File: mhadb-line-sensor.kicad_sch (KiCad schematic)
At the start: 93 parts, among them J1 Conn_01x04, J2 TC2030, J3 Conn_01x04_Pin, J4 Conn_01x04_Pin, SW1 SW_Push, SW2 SW_Push, SW3 SW_Push, SW4 SW_Push, U1 STM32F103C8Tx, U10 QRE1113GR, U11 QRE1113GR, U12 QRE1113GR, U2 QRE1113GR, U3 SN65HVD230, U4 QRE1113GR, U5 QRE1113GR, U6 QRE1113GR, U7 QRE1113GR, U8 QRE1113GR, U9 QRE1113GR, Y1 8M

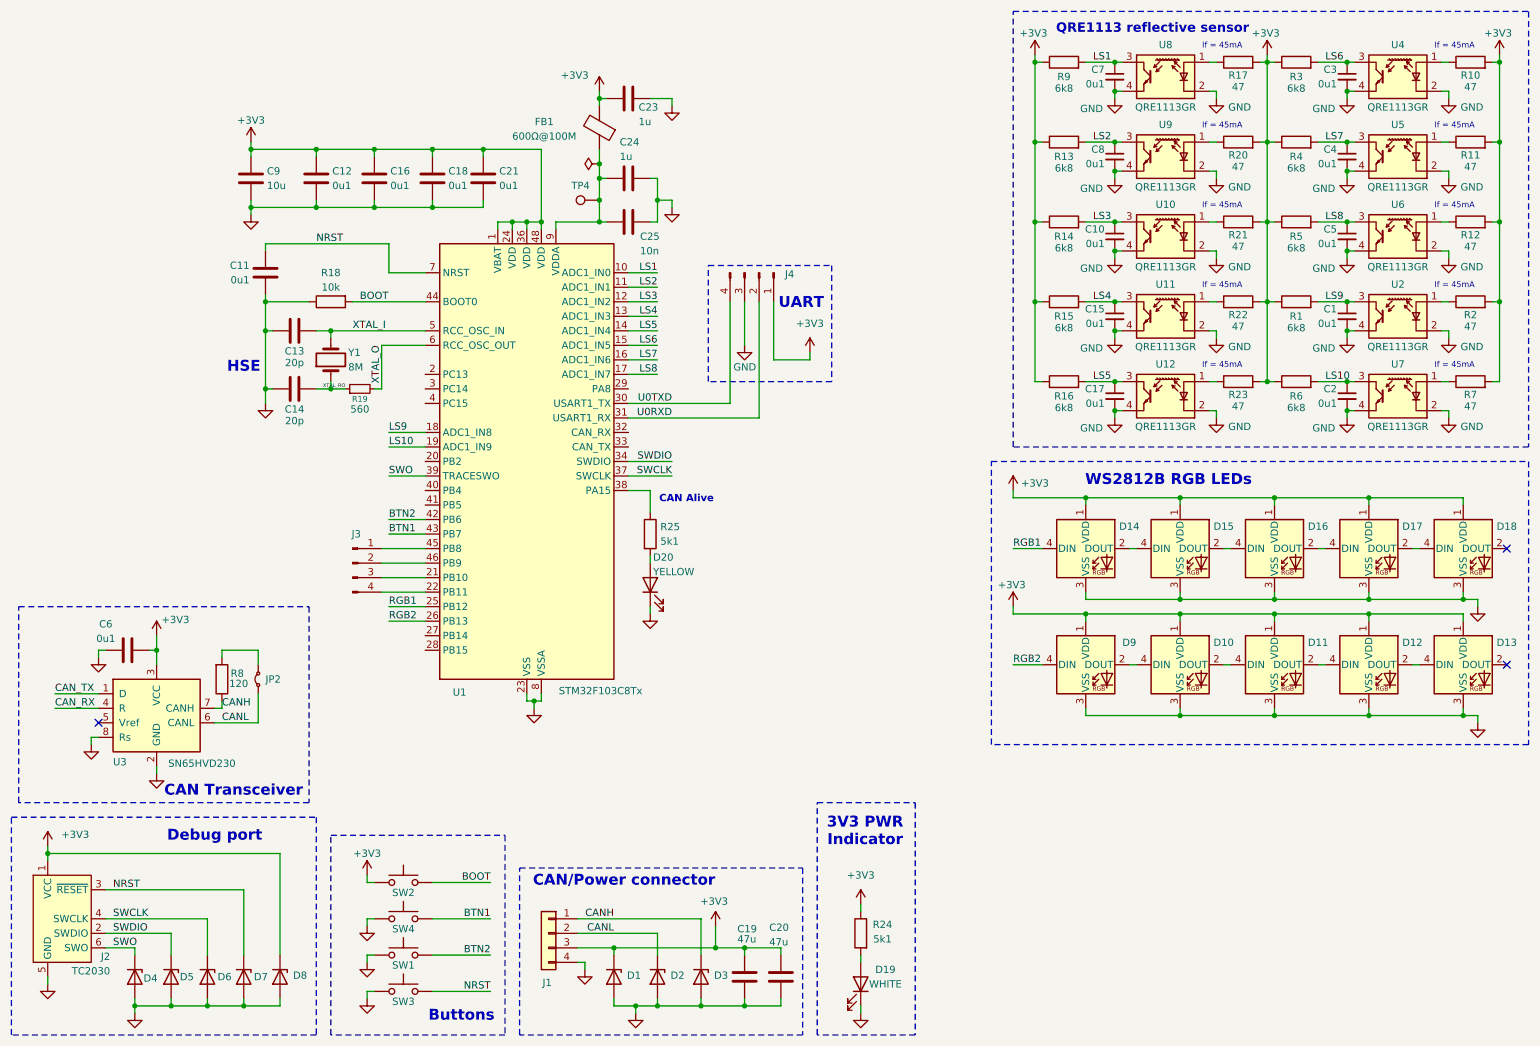
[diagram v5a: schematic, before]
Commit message: schem: switch to 5v architecture and add 3v3 LDO
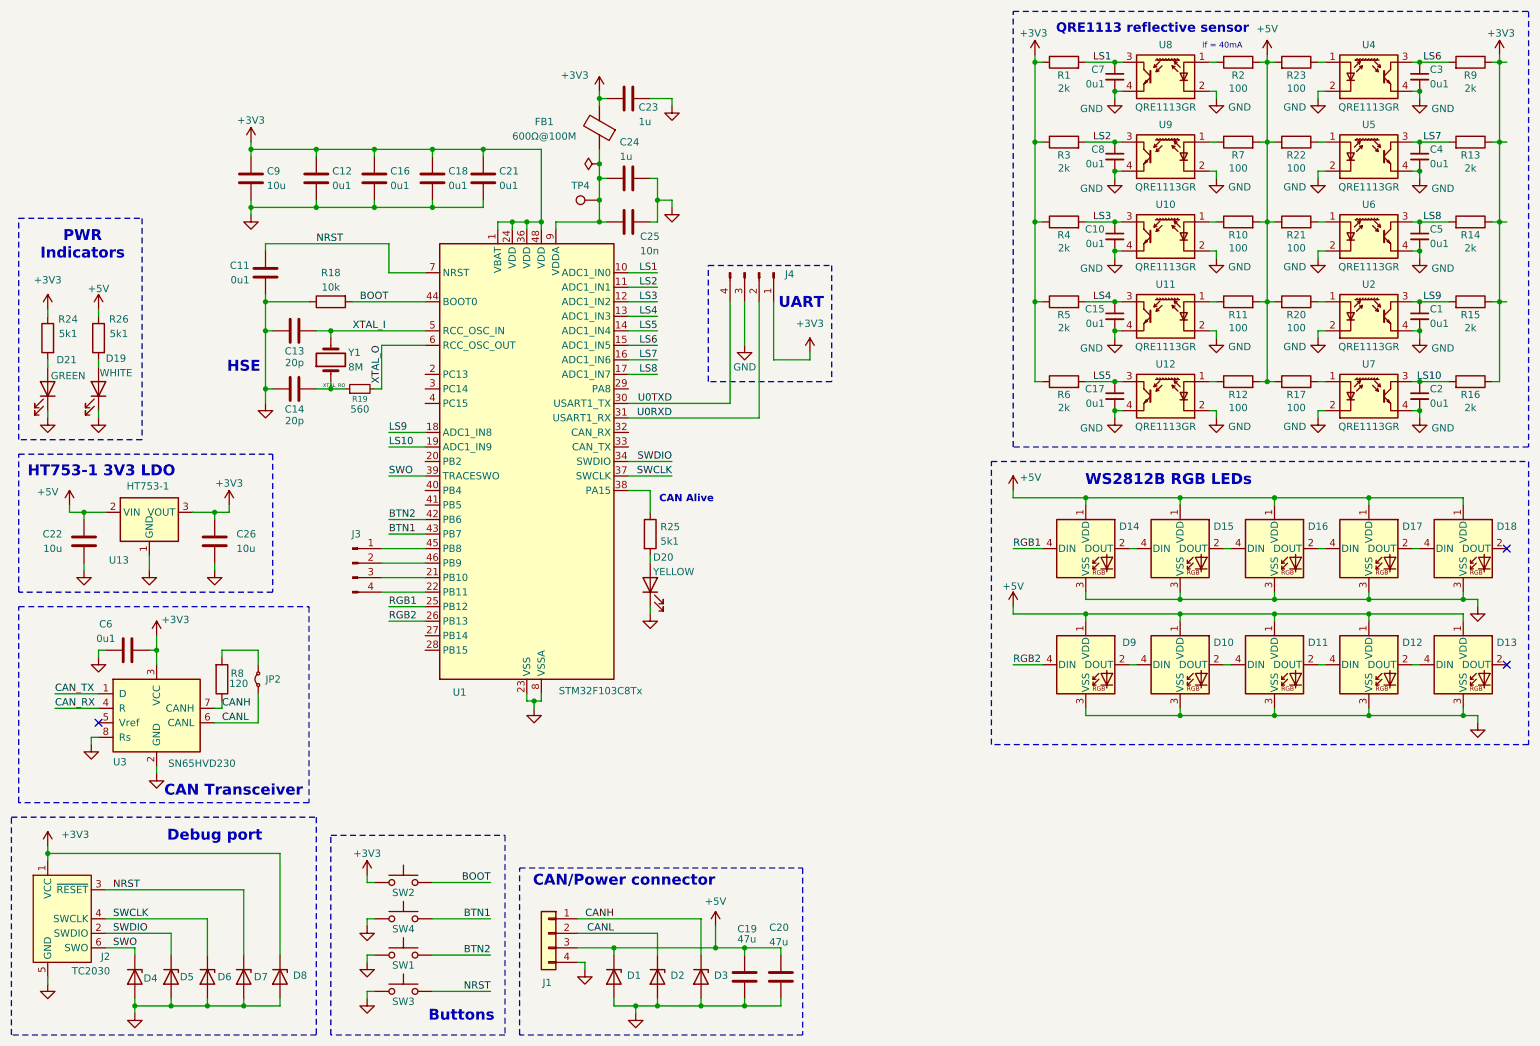
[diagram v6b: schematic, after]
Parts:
- added C22, C26: 10u, Capacitor_SMD:C_0805_2012Metric, symbol Device:C
- added D21: GREEN, LED_SMD:LED_0805_2012Metric, symbol Device:LED
- added R26: 5k1, Resistor_SMD:R_0402_1005Metric, symbol Device:R
- added U13: HT753-1, Package_TO_SOT_SMD:SOT-89-3, symbol Regulator_Linear:HT75xx-1-SOT89
- R1, R13, R14, R15, R16, R3, R4, R5, R6, R9: value 6k8 -> 2k; JLCPCB Part # C23212 -> C4190; Manufacturer Part Number 0603WAF6801T5E -> 0603WAF2201T5E
- R10, R11, R12, R17, R2, R20, R21, R22, R23, R7: value 47 -> 100; footprint Resistor_SMD:R_0603_1608Metric -> Capacitor_SMD:C_1206_3216Metric; JLCPCB Part # C23182 -> C17901; Manufacturer Part Number 0603WAF470JT5E -> 1206W4F1000T5E
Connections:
- net +3V3: now also C26.1, U13.3 (VOUT); no longer C19.1, C20.1, D1.1 (K), D10.1 (VDD), D11.1 (VDD), D12.1 (VDD), D13.1 (VDD), D14.1 (VDD), D15.1 (VDD), D16.1 (VDD), D17.1 (VDD), D18.1 (VDD), D9.1 (VDD), J1.3 (Pin_3), R10.2, R11.2, R12.2, R17.2, R2.2, R20.2, R21.2, R22.2, R23.2, R7.2
- net GND: now also C22.2, C26.2, D21.1 (K), U13.1 (GND)
- net LS1: now also R1.2; no longer R9.2
- net LS10: now also R16.2; no longer R6.2
- net LS2: now also R3.2; no longer R13.2
- net LS3: now also R4.2; no longer R14.2
- net LS4: now also R5.2; no longer R15.2
- net LS5: now also R6.2; no longer R16.2
- net LS6: now also R9.2; no longer R3.2
- net LS7: now also R13.2; no longer R4.2
- net LS8: now also R14.2; no longer R5.2
- net LS9: now also R15.2; no longer R1.2
- net at R23.1: now also U4.1 (A); no longer U12.1 (A)
- net at R10.1: now also U10.1 (A); no longer U4.1 (A)
- net at D19.2 (A): now also R26.2; no longer R24.2
- net at U2.1 (A): now also R20.1; no longer R2.1
- net at R22.1: now also U5.1 (A); no longer U11.1 (A)
- net at R11.1: now also U11.1 (A); no longer U5.1 (A)
- net at R12.1: now also U12.1 (A); no longer U6.1 (A)
- net at R21.1: now also U6.1 (A); no longer U10.1 (A)
- net at U8.1 (A): now also R2.1; no longer R17.1
- net at U9.1 (A): now also R7.1; no longer R20.1
- net at U7.1 (A): now also R17.1; no longer R7.1
- new net: D21.2 (A), R24.2
- new net +5V: C19.1, C20.1, C22.1, D1.1 (K), D10.1 (VDD), D11.1 (VDD), D12.1 (VDD), D13.1 (VDD), D14.1 (VDD), D15.1 (VDD), D16.1 (VDD), D17.1 (VDD), D18.1 (VDD), D9.1 (VDD), J1.3 (Pin_3), R10.2, R11.2, R12.2, R17.2, R2.2, R20.2, R21.2, R22.2, R23.2, R26.1, R7.2, U13.2 (VIN)
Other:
- note added: "HT753-1 3V3 LDO"
- note added: "If = 40mA"
- note added: "PWR Indicators"
- note removed: "3V3 PWR Indicator"
- note removed: "If = 45mA"
- moved on the sheet: C1, C2, C3, C4, C5, D19, R24, U2, U4, U5, U6, U7

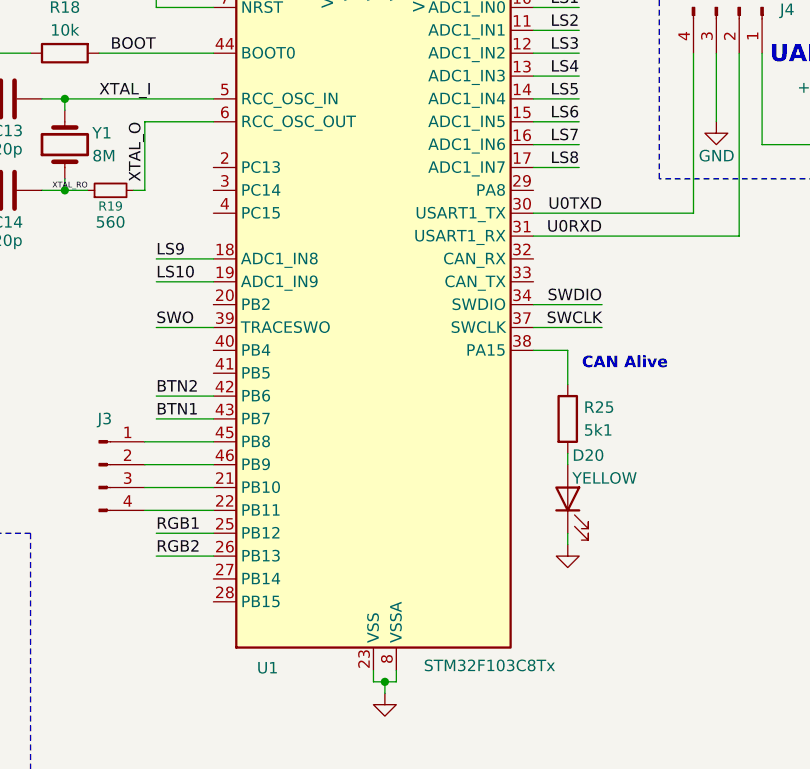
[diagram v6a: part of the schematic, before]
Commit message: schem: add no connects
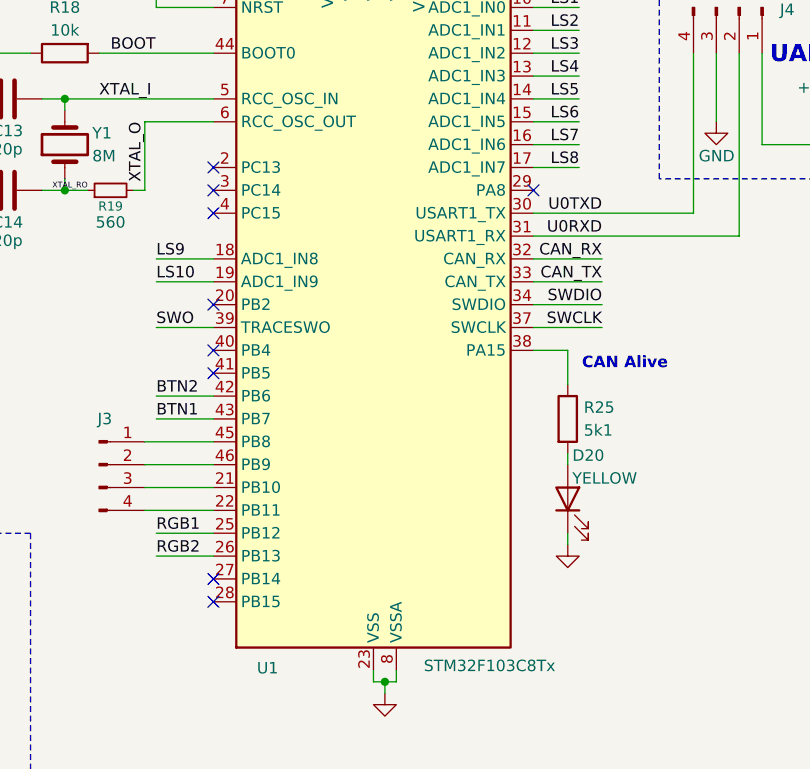
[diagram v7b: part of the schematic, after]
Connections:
- net CAN_RX: now also U1.32 (PA11)
- net CAN_TX: now also U1.33 (PA12)
- no-connect marks 3 -> 12
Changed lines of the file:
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@@
 	)
 	(no_connect
+		(at 87.63 82.55)
+	)
+	(no_connect
+		(at 87.63 85.09)
+	)
+	(no_connect
+		(at 87.63 102.87)
+	)
+	(no_connect
+		(at 123.19 82.55)
+	)
+	(no_connect
 		(at 276.86 130.81)
 	)
 	(no_connect
+		(at 87.63 100.33)
+	)
+	(no_connect
 		(at 30.48 140.97)
 	)
 	(no_connect
+		(at 87.63 80.01)
+	)
+	(no_connect
 		(at 276.86 110.49)
 	)
+	(no_connect
+		(at 87.63 128.27)
+	)
+	(no_connect
+		(at 87.63 125.73)
+	)
+	(no_connect
+		(at 87.63 95.25)
+	)
 	(wire
 		(pts
@@
 	(wire
 		(pts
+			(xy 130.81 92.71) (xy 123.19 92.71)
+		)
+		(stroke
+			(width 0)
+			(type default)
+		)
+	)
+	(wire
+		(pts
 			(xy 194.31 67.31) (xy 195.58 67.31)
 		)
@@
 	(wire
 		(pts
+			(xy 130.81 90.17) (xy 123.19 90.17)
+		)
+		(stroke
+			(width 0)
+			(type default)
+		)
+	)
+	(wire
+		(pts
 			(xy 81.28 92.71) (xy 87.63 92.71)
 		)
@@
 	)
 	(label "CAN_RX"
+		(at 130.81 90.17 180)
+		(effects
+			(font
+				(size 1.27 1.27)
+			)
+			(justify right bottom)
+		)
+	)
+	(label "CAN_RX"
 		(at 22.86 138.43 0)
 		(effects
@@
 		(effects
 			(font
+				(size 1.27 1.27)
+			)
+			(justify right bottom)
+		)
+	)
+	(label "CAN_TX"
+		(at 130.81 92.71 180)
+		(effects
+			(font

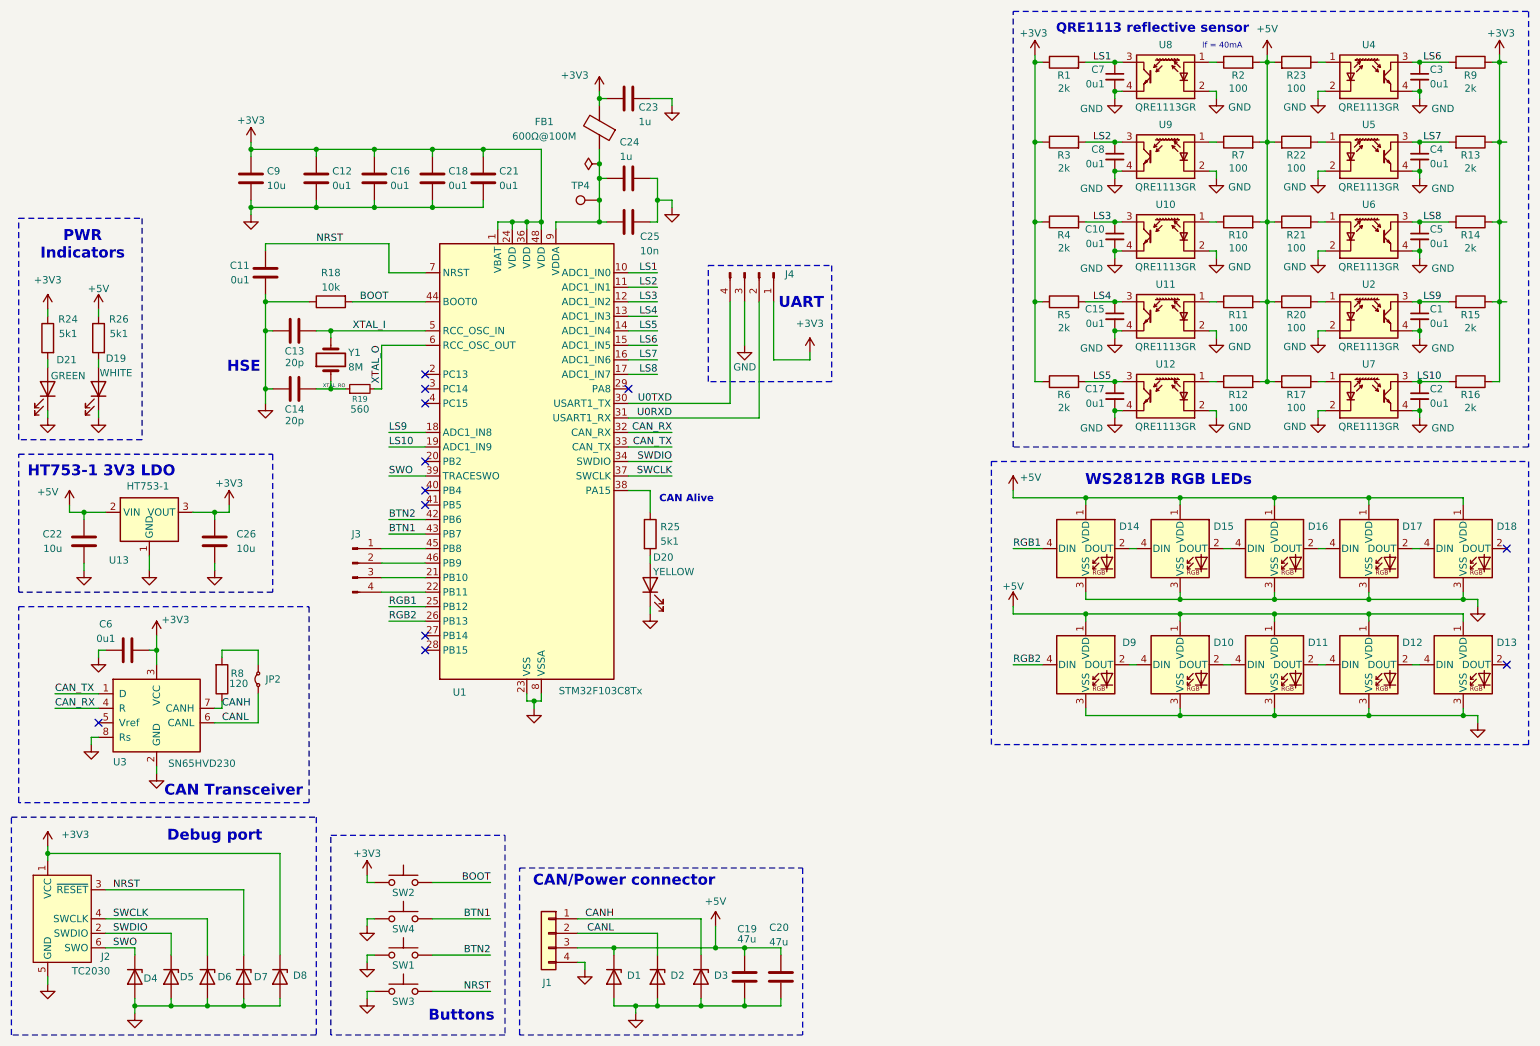
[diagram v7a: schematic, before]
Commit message: schem: add test points
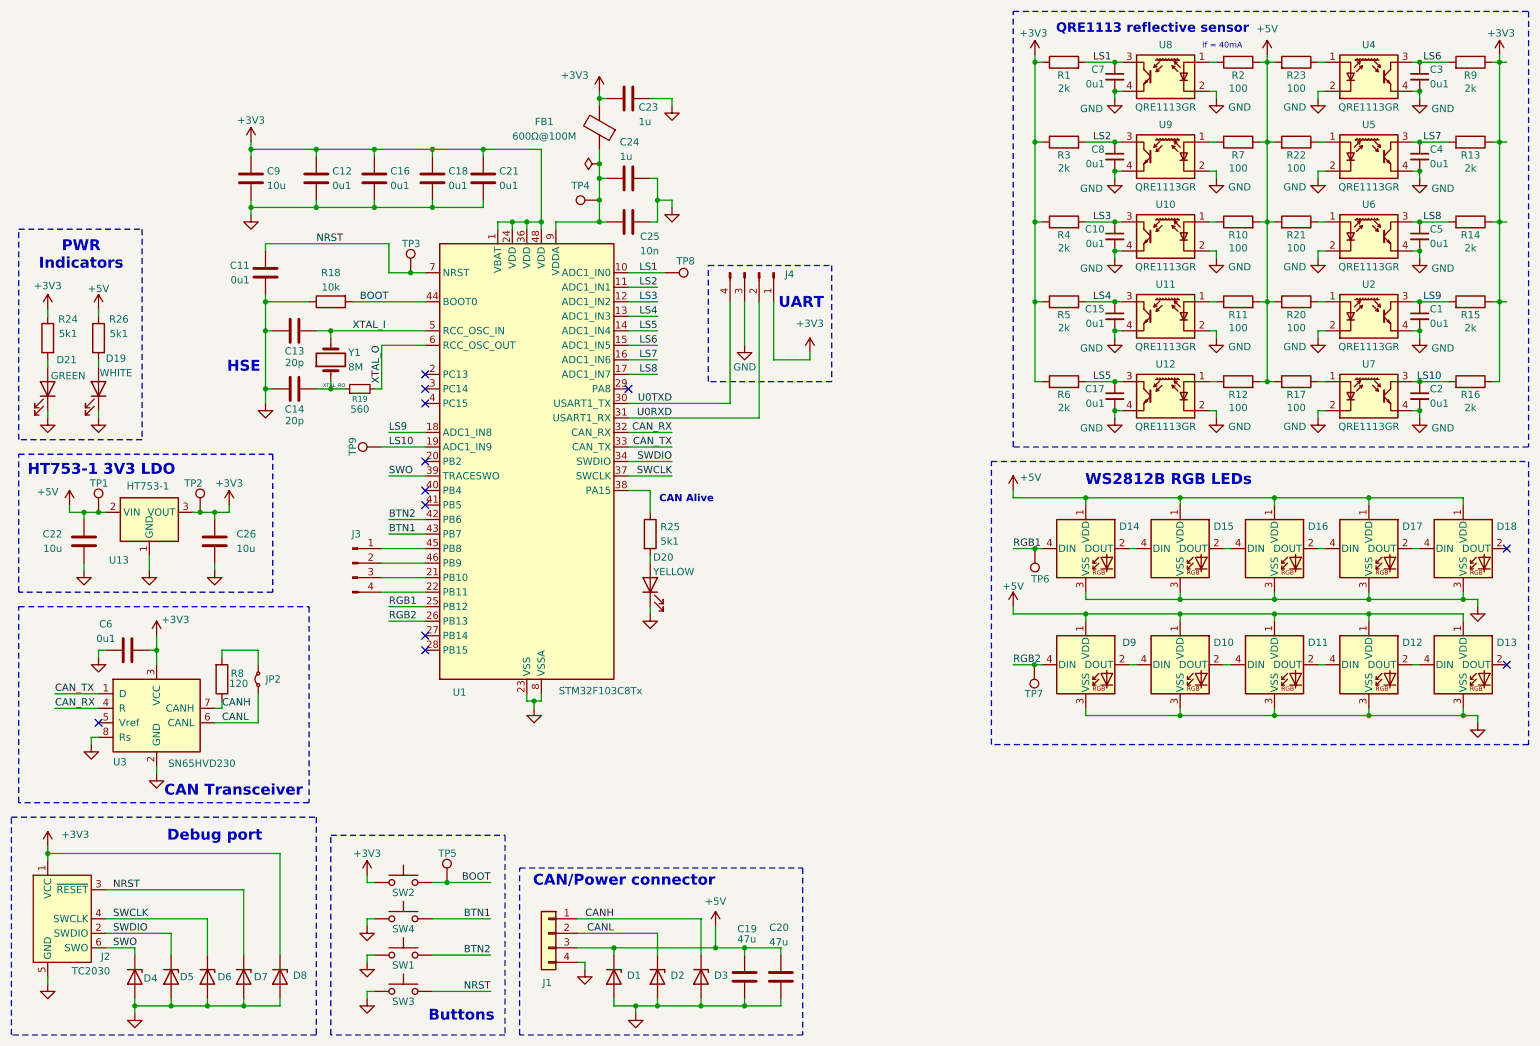
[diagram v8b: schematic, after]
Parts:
- added TP1, TP2, TP3, TP5, TP6, TP7, TP8, TP9: TestPoint, TestPoint:TestPoint_Pad_D2.0mm, symbol Connector:TestPoint
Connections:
- net +3V3: now also TP2.1
- net +5V: now also TP1.1
- net BOOT: now also TP5.1
- net LS1: now also TP8.1
- net LS10: now also TP9.1
- net NRST: now also TP3.1
- net RGB1: now also TP6.1
- net RGB2: now also TP7.1
